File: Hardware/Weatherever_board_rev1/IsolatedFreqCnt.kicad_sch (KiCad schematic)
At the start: 26 parts

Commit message: Finished HW schematic and minor project cleanup
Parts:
- removed C?: 100n, Capacitor_SMD:C_0805_2012Metric_Pad1.18x1.45mm_HandSolder, symbol Device:C_Small
- removed R?: 270, Resistor_SMD:R_0805_2012Metric_Pad1.20x1.40mm_HandSolder, symbol Device:R_Small
- removed U? (x2): H11L3, Package_DIP:SMDIP-6_W7.62mm, symbol Isolator:H11L3
- added C303: 100n, Capacitor_SMD:C_0805_2012Metric_Pad1.18x1.45mm_HandSolder, symbol Device:C_Small
- added R310: 3k3, Resistor_SMD:R_0805_2012Metric_Pad1.20x1.40mm_HandSolder, symbol Device:R_Small
- added U301, U303: 6N137, Package_DIP:SMDIP-6_W7.62mm, symbol Isolator:6N137
- R303: renamed from R?; value 270 -> 3k3
- gave numbers to parts that had none: 19
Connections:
- net +3V3: now also C303.1, R310.1, U301.8 (VCC), U303.8 (VCC)
- net CNT_IN: now also U301.6 (VO), U301.7 (EN)
- net CONN_VALID: now also R310.2, U303.6 (VO), U303.7 (EN)
- net GNDD: now also C303.2, U301.5 (GND), U303.5 (GND)
- net at C304.1, R312.1, U302.1: now also U303.3 (C)
- net at C302.1, R307.1, U302.7: now also U301.3 (C)
- net at R311.2: now also U303.2 (A)
- net at R306.2: now also U301.2 (A)
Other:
- moved on the sheet: C301, R303

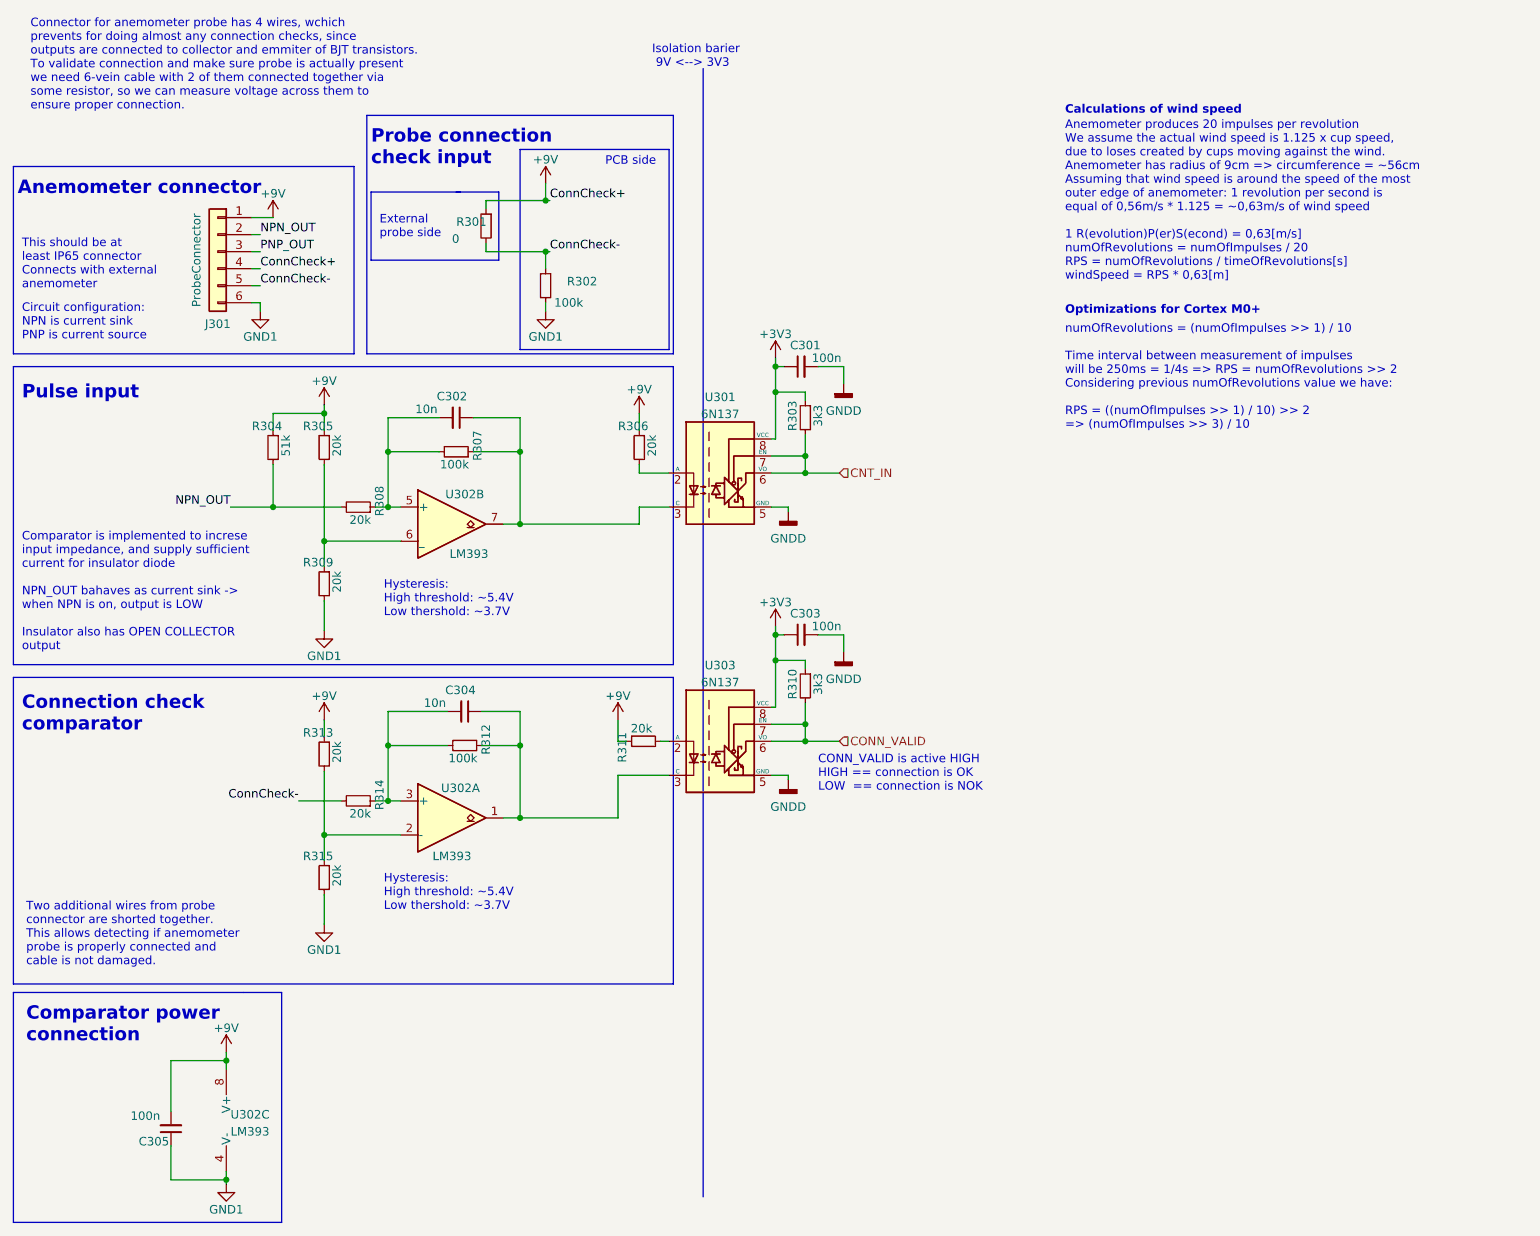
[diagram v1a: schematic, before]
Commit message: New hw element and CommHandler tests
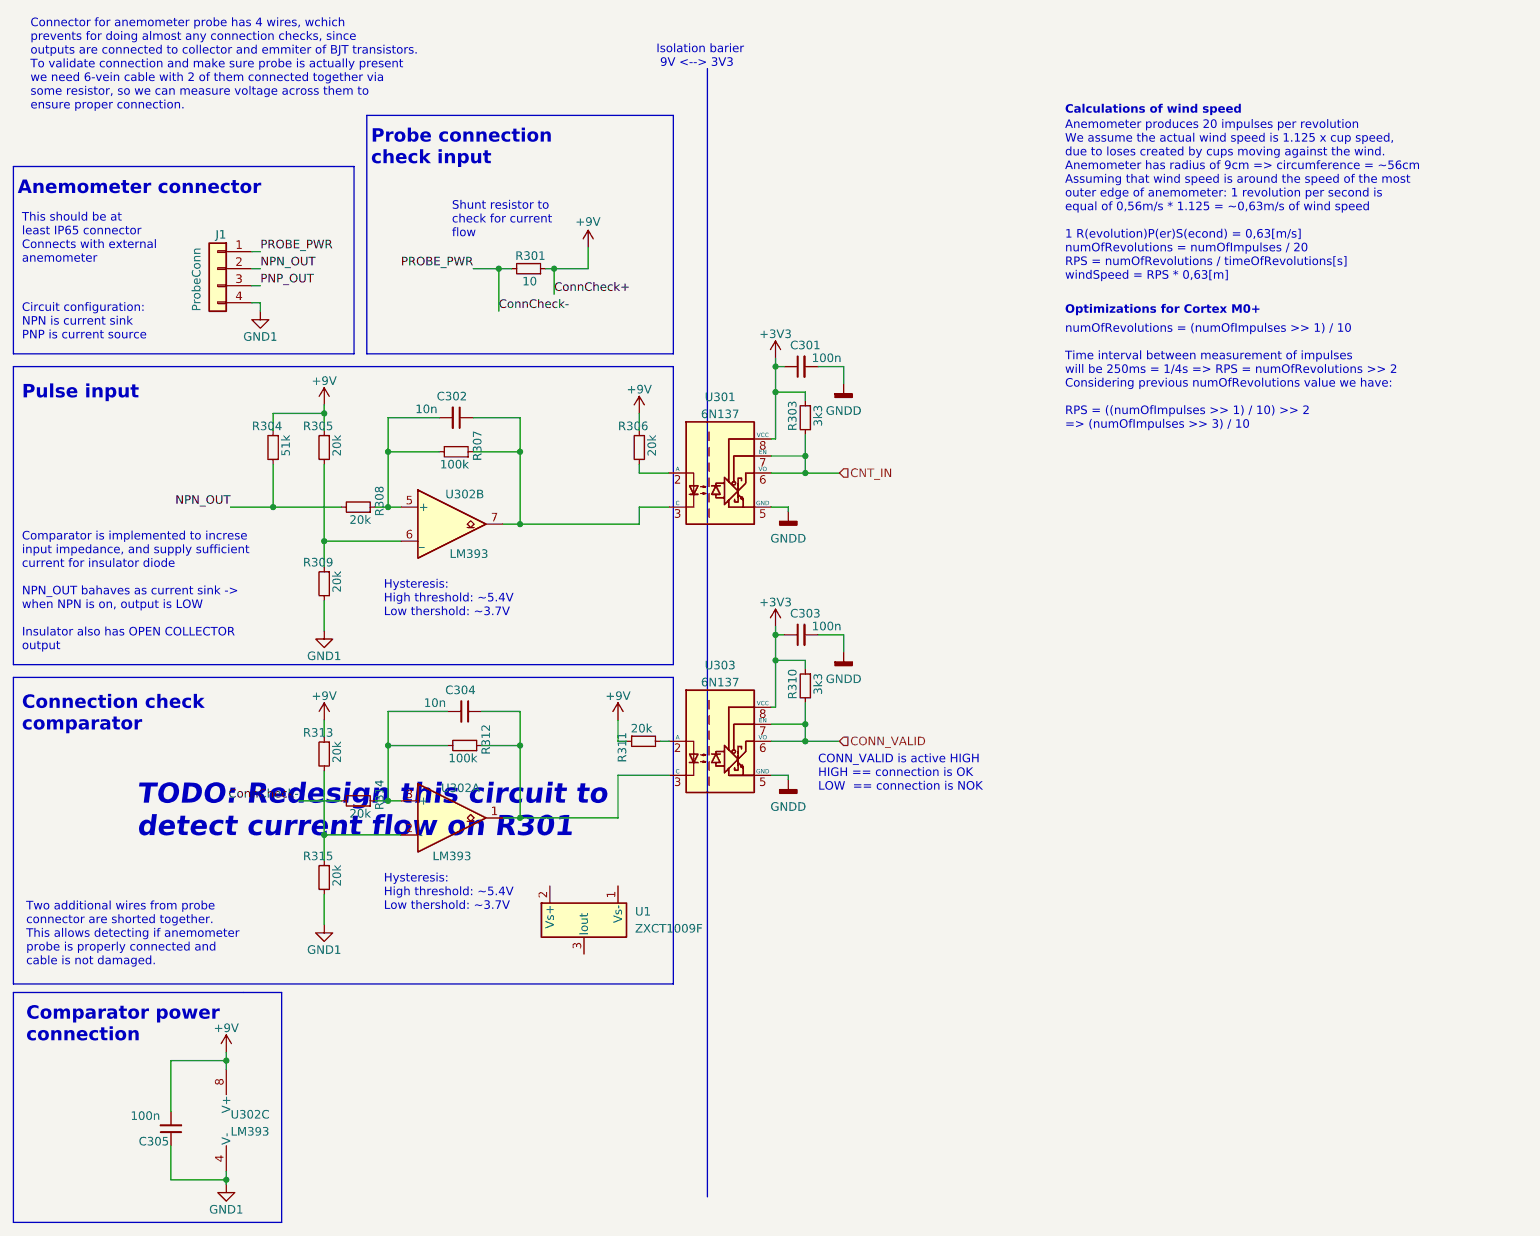
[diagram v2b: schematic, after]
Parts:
- removed J301: ProbeConnector, symbol Connector_Generic:Conn_01x06
- removed R302: 100k, symbol Device:R_Small
- added J1: ProbeConn, symbol Connector_Generic:Conn_01x04
- added U1: ZXCT1009F, Package_TO_SOT_SMD:SOT-23, symbol Amplifier_Current:ZXCT1009F
- R301: value 0 -> 10
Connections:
- net ConnCheck-: now also J1.1 (Pin_1)
- net GND1: now also J1.4 (Pin_4)
- net NPN_OUT: now also J1.2 (Pin_2)
- net PNP_OUT: now also J1.3 (Pin_3)
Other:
- note added: "Shunt resistor to check for current flow"
- note added: "TODO: Redesign this circuit to detect current flow on R301"
- note removed: "External probe side"
- note removed: "PCB side"
- moved on the sheet: R301

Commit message: Funished schematics and GPIO drv interface
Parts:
- added R302: 2k, Resistor_SMD:R_0805_2012Metric_Pad1.20x1.40mm_HandSolder, symbol Device:R_Small
- R301: value 10 -> 330
- R313: value 20k -> 51k
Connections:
- net +9V: now also U1.2 (Vs+)
- net ConnCheck-: now also U1.1 (Vs-); no longer R314.2
- net GND1: now also R302.2
- net CurrentOut: now reaches U1.3 (Iout)
- net CurrentOut: now also R314.2, R302.1
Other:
- note added: "Hysteresis: High threshold: ~3.1V Low thershold: ~1.2V"
- note removed: "TODO: Redesign this circuit to detect current flow on R301"
- note removed: "Two additional wires from probe connector are shorted together. This allows detecting if anemometer probe is properly connected and cable is not damaged."
- moved on the sheet: U1
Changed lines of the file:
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@@
   (junction (at 146.685 120.65) (diameter 0) (color 0 0 0 0)
   )
+  (junction (at 47.625 145.415) (diameter 0) (color 0 0 0 0)
+  )
   (junction (at 146.685 123.19) (diameter 0) (color 0 0 0 0)
   )
@@
     (stroke (width 0) (type default))
   )
+  (wire (pts (xy 49.53 130.81) (xy 52.705 130.81))
+    (stroke (width 0) (type default))
+  )
   (wire (pts (xy 104.14 118.745) (xy 104.14 123.825))
     (stroke (width 0) (type default))
@@
     (stroke (width 0) (type default))
   )
+  (wire (pts (xy 47.625 151.13) (xy 47.625 152.4))
+    (stroke (width 0) (type default))
+  )
   (wire (pts (xy 143.51 107.315) (xy 142.24 107.315))
     (stroke (width 0) (type default))
@@
     (stroke (width 0) (type default))
   )
+  (wire (pts (xy 52.705 130.81) (xy 52.705 133.35))
+    (stroke (width 0) (type default))
+  )
   (polyline (pts (xy 28.575 160.655) (xy 28.575 194.945))
     (stroke (width 0) (type default))
@@
     (stroke (width 0) (type default))
   )
-  (wire (pts (xy 71.12 132.08) (xy 77.47 132.08))
+  (wire (pts (xy 73.66 132.08) (xy 77.47 132.08))
     (stroke (width 0) (type default))
   )
@@
     (stroke (width 0) (type default))
   )
+  (wire (pts (xy 45.72 128.905) (xy 45.72 130.81))
+    (stroke (width 0) (type default))
+  )
   (wire (pts (xy 74.93 73.025) (xy 74.93 74.295))
     (stroke (width 0) (type default))
   )
+  (wire (pts (xy 47.625 143.51) (xy 47.625 145.415))
+    (stroke (width 0) (type default))
+  )
   (wire (pts (xy 142.24 78.105) (xy 141.605 78.105))
     (stroke (width 0) (type default))
@@
     (stroke (width 0) (type default))
   )
+  (wire (pts (xy 47.625 145.415) (xy 50.165 145.415))
+    (stroke (width 0) (type default))
+  )
   (wire (pts (xy 146.685 123.19) (xy 151.765 123.19))
     (stroke (width 0) (type default))
   )
+  (wire (pts (xy 42.545 130.81) (xy 42.545 133.35))
+    (stroke (width 0) (type default))
+  )
   (wire (pts (xy 60.325 188.595) (xy 60.325 189.23))
     (stroke (width 0) (type default))
@@
     (stroke (width 0) (type default))
   )
+  (wire (pts (xy 49.53 128.905) (xy 49.53 130.81))
+    (stroke (width 0) (type default))
+  )
   (wire (pts (xy 84.455 132.08) (xy 86.36 132.08))
     (stroke (width 0) (type default))
@@
     (stroke (width 0) (type default))
   )
+  (wire (pts (xy 47.625 145.415) (xy 47.625 146.05))
+    (stroke (width 0) (type default))
+  )
   (wire (pts (xy 74.93 137.16) (xy 74.93 140.97))
     (stroke (width 0) (type default))
@@
   )
   (wire (pts (xy 146.685 112.395) (xy 146.685 111.125))
+    (stroke (width 0) (type default))
+  )
+  (wire (pts (xy 45.72 130.81) (xy 42.545 130.81))
     (stroke (width 0) (type default))
   )
@@
     (effects (font (size 1.27 1.27)) (justify left bottom))
   )
-  (text "Two additional wires from probe\nconnector are shorted together.\nThis allows detecting if anemometer\nprobe is properly connected and\ncable is not damaged."
-    (at 30.48 156.845 0)
-    (effects (font (size 1.27 1.27)) (justify left bottom))
-  )
   (text "Probe connection \ncheck input" (at 81.915 37.465 0)
     (effects (font (size 2 2) (thickness 0.4) bold) (justify left bottom))
@@
     (effects (font (size 1.27 1.27)) (justify left bottom))
   )
-  (text "Hysteresis:\nHigh threshold: ~5.4V\nLow thershold: ~3.7V"
+  (text "Hysteresis:\nHigh threshold: ~3.1V\nLow thershold: ~1.2V"
     (at 83.82 148.59 0)
     (effects (font (size 1.27 1.27)) (justify left bottom))
@@
     (effects (font (size 1.27 1.27)) (justify left bottom))
   )
-  (text "TODO: Redesign this circuit to\ndetect current flow on R301"
-    (at 46.99 137.795 0)
-    (effects (font (size 3 3) (thickness 0.508) bold italic (color 255 65 58 1)) (justify left bottom))
-  )
   (text "This should be at \nleast IP65 connector\nConnects with external \nanemometer"
     (at 29.845 52.07 0)
@@
     (effects (font (size 1.27 1.27)) (justify left bottom))
   )
-  (label "ConnCheck-" (at 71.12 132.08 180) (fields_autoplaced)
+  (label "ConnCheck+" (at 45.72 128.905 180) (fields_autoplaced)
     (effects (font (size 1.27 1.27)) (justify right bottom))
   )
+  (label "CurrentOut" (at 50.165 145.415 0) (fields_autoplaced)
+    (effects (font (size 1.27 1.27)) (justify left bottom))
+  )
+  (label "ConnCheck-" (at 49.53 128.905 0) (fields_autoplaced)
+    (effects (font (size 1.27 1.27)) (justify left bottom))
+  )
   (label "ConnCheck-" (at 100.965 59.055 0) (fields_autoplaced)
     (effects (font (size 1.27 1.27)) (justify left bottom))
@@
   (label "PROBE_PWR" (at 65.405 50.165 0) (fields_autoplaced)
     (effects (font (size 1.27 1.27)) (justify left bottom))
+  )
+  (label "CurrentOut" (at 73.66 132.08 180) (fields_autoplaced)
+    (effects (font (size 1.27 1.27)) (justify right bottom))
   )
   (label "NPN_OUT" (at 65.405 52.705 0) (fields_autoplaced)
@@
       (effects (font (size 1.27 1.27)) (justify right))
     )
-    (property "Value" "20k" (at 76.835 123.19 90)
+    (property "Value" "51k" (at 76.835 123.19 90)
       (effects (font (size 1.27 1.27)) (justify right))
     )
@@
         (path "/e63e39d7-6ac0-4ffd-8aa3-1841a4541b55/3b0f90e8-57d9-42d7-85e4-9d338a5720fc"
           (reference "#PWR0301") (unit 1)
+        )
+      )
+    )
+  )
+  (symbol (lib_id "power:GND1") (at 47.625 152.4 0) (unit 1)
+    (in_bom yes) (on_board yes) (dnp no)
+    (property "Reference" "#PWR0302" (at 47.625 158.75 0)
+      (effects (font (size 1.27 1.27)) hide)
+    )
+    (property "Value" "GND1" (at 47.625 156.21 0)
+      (effects (font (size 1.27 1.27)))
+    )
+    (property "Footprint" "" (at 47.625 152.4 0)
+      (effects (font (size 1.27 1.27)) hide)
+    )
+    (property "Datasheet" "" (at 47.625 152.4 0)
+      (effects (font (size 1.27 1.27)) hide)
+    )
+    (pin "1")
+    (instances
+      (project "Weatherever_board_rev1"
+        (path "/e63e39d7-6ac0-4ffd-8aa3-1841a4541b55/3b0f90e8-57d9-42d7-85e4-9d338a5720fc"
+          (reference "#PWR0302") (unit 1)
         )
       )
@@
   (symbol (lib_id "Device:R_Small") (at 122.555 123.19 90) (mirror x) (unit 1)
     (in_bom yes) (on_board yes) (dnp no)
-    (property "Reference" "R311" (at 119.38 126.365 0)
+    (property "Reference" "R311" (at 120.015 125.095 90)
       (effects (font (size 1.27 1.27)) (justify right))
     )
@@
     )
   )
-  (symbol (lib_id "Amplifier_Current:ZXCT1009F") (at 113.665 149.86 0) (unit 1)
+  (symbol (lib_id "Amplifier_Current:ZXCT1009F") (at 47.625 138.43 0) (unit 1)
     (in_bom yes) (on_board yes) (dnp no) (fields_autoplaced)
-    (property "Reference" "U1" (at 121.285 148.59 0)
+    (property "Reference" "U1" (at 55.245 137.16 0)
       (effects (font (size 1.27 1.27)) (justify left))
     )
-    (property "Value" "ZXCT1009F" (at 121.285 151.13 0)
+    (property "Value" "ZXCT1009F" (at 55.245 139.7 0)
       (effects (font (size 1.27 1.27)) (justify left))
     )
-    (property "Footprint" "Package_TO_SOT_SMD:SOT-23" (at 113.665 149.86 0)
-      (effects (font (size 1.27 1.27)) hide)
-    )
-    (property "Datasheet" "https://www.diodes.com/assets/Datasheets/ZXCT1009.pdf" (at 112.395 149.86 0)
+    (property "Footprint" "Package_TO_SOT_SMD:SOT-23" (at 47.625 138.43 0)
+      (effects (font (size 1.27 1.27)) hide)
+    )
+    (property "Datasheet" "https://www.diodes.com/assets/Datasheets/ZXCT1009.pdf" (at 46.355 138.43 0)
       (effects (font (size 1.27 1.27)) hide)
     )
@@
       (effects (font (size 1.27 1.27)) (justify right))
     )
-    (property "Value" "10" (at 106.68 54.61 90)
+    (property "Value" "330" (at 106.68 54.61 90)
       (effects (font (size 1.27 1.27)) (justify right))
     )
@@
         )
       )
+    )
+  )
+  (symbol (lib_id "Device:R_Small") (at 47.625 148.59 0) (mirror y) (unit 1)
+    (in_bom yes) (on_board yes) (dnp no)
+    (property "Reference" "R302" (at 41.275 148.59 0)
+      (effects (font (size 1.27 1.27)) (justify right))
+    )
+    (property "Value" "2k" (at 49.53 146.685 90)
+      (effects (font (size 1.27 1.27)) (justify right))
+    )
+    (property "Footprint" "Resistor_SMD:R_0805_2012Metric_Pad1.20x1.40mm_HandSolder" (at 47.625 148.59 0)
+      (effects (font (size 1.27 1.27)) hide)
+    )
+    (property "Datasheet" "~" (at 47.625 148.59 0)
+      (effects (font (size 1.27 1.27)) hide)
+    )
+    (pin "1")
+    (pin "2")
+    (instances
+      (project "Weatherever_board_rev1"
+        (path "/e63e39d7-6ac0-4ffd-8aa3-1841a4541b55/3b0f90e8-57d9-42d7-85e4-9d338a5720fc"
+          (reference "R302") (unit 1)
+        )
+      )
